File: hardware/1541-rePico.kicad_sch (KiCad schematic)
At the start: 10 parts, among them J1 Display Connector, J2 KEYS, J3 RESET_1541, J4 SD Card Module Connector, J5 EXT_5V, SW1 RESET, U1 Pico

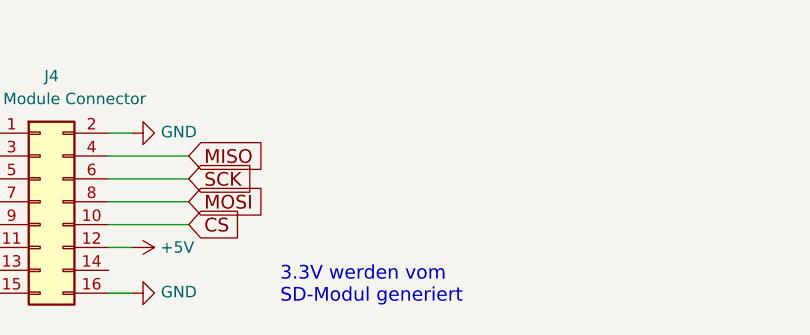
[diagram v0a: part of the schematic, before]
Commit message: updated PCB layout
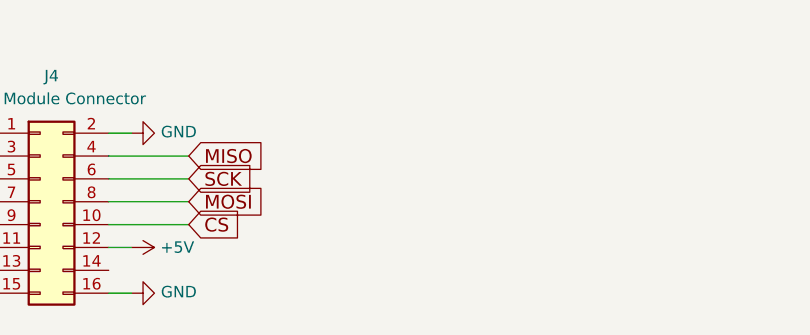
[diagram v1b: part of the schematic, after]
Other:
- note removed: "3.3V werden vom SD-Modul generiert"
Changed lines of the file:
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@@
     (stroke (width 0) (type default))
-  )
-  (text "3.3V werden vom\nSD-Modul generiert" (at 138.43 184.15 0)
-    (effects (font (size 1.524 1.524)) (justify left bottom))
   )
   (text "Jumper Normal offen" (at 241.3 105.41 0)

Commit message: updated schematics&pcb - version 1.1
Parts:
- removed J2: KEYS, Connector_PinHeader_2.54mm:PinHeader_1x04_P2.54mm_Vertical, symbol Connector_Generic:Conn_01x04
- added J2: Conn_02x03_Odd_Even, Connector_PinHeader_2.54mm:PinHeader_2x03_P2.54mm_Vertical, symbol Connector_Generic:Conn_02x03_Odd_Even
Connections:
- net BT1: now also J2.2 (Pin_2)
- net BT2: now also J2.4 (Pin_4)
- net BT3: now also J2.6 (Pin_6)
- net GND: now also J2.1 (Pin_1), J2.3 (Pin_3), J2.5 (Pin_5)

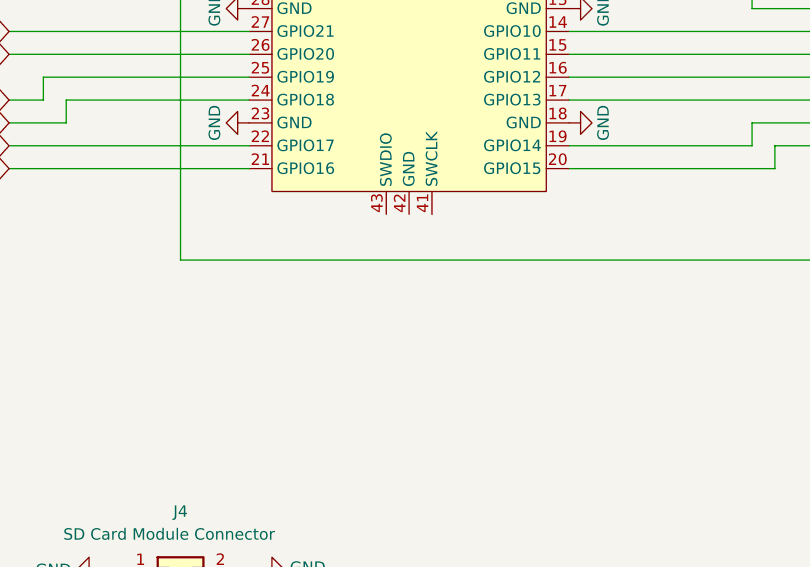
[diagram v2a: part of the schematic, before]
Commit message: fix WPS cross-driving
connection between 1541-board and VIA cut off
no cross driving of existing 74LS04 and Pico avoided
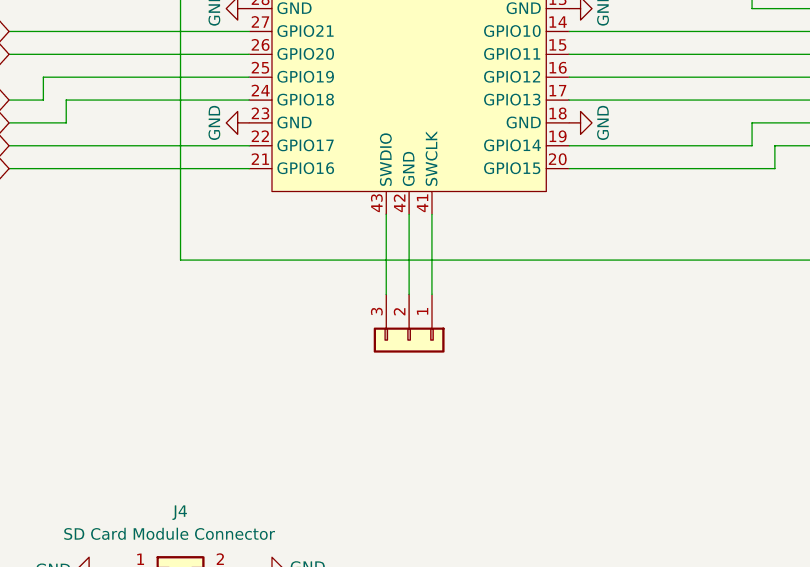
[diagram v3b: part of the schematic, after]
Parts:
- added SWDBG1: DEBUG, Connector_PinHeader_2.54mm:PinHeader_1x03_P2.54mm_Vertical, symbol Connector_Generic:Conn_01x03
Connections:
- net at U1.41 (SWCLK): now also SWDBG1.1 (Pin_1)
- net at U1.42 (GND): now also SWDBG1.2 (Pin_2)
- net at U1.43 (SWDIO): now also SWDBG1.3 (Pin_3)
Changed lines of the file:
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@@
+	(wire
+		(pts
+			(xy 140.97 125.73) (xy 140.97 134.62)
+		)
+		(stroke
+			(width 0)
+			(type default)
+		)
+	)
 	(wire
 		(pts
@@
 	(wire
 		(pts
+			(xy 138.43 125.73) (xy 138.43 134.62)
+		)
+		(stroke
+			(width 0)
+			(type default)
+		)
+	)
+	(wire
+		(pts
 			(xy 106.68 170.18) (xy 97.79 170.18)
 		)
@@
 		(pts
 			(xy 229.87 95.25) (xy 219.71 95.25)
+		)
+		(stroke
+			(width 0)
+			(type default)
+		)
+	)
+	(wire
+		(pts
+			(xy 135.89 125.73) (xy 135.89 134.62)
 		)
 		(stroke
@@
 					(unit 1)
 				)
+			)
+		)
+	)
+	(symbol
+		(lib_id "Connector_Generic:Conn_01x03")
+		(at 138.43 139.7 270)
+		(unit 1)
+		(exclude_from_sim no)
+		(in_bom yes)
+		(on_board yes)
+		(dnp no)
+		(property "Reference" "SWDBG1"
+			(at 143.51 139.7 90)
+			(effects
+				(font
+					(size 1.27 1.27)
+				)
+				(justify left)
+				(hide yes)
+			)
+		)
+		(property "Value" "DEBUG"
+			(at 138.43 142.24 90)
+			(effects
+				(font
+					(size 1.27 1.27)
+				)
+				(justify left)
+				(hide yes)
+			)
+		)
+		(property "Footprint" "Connector_PinHeader_2.54mm:PinHeader_1x03_P2.54mm_Vertical"
+			(at 138.43 139.7 0)
+			(effects
+				(font
+					(size 1.27 1.27)
+				)
+				(hide yes)
+			)
+		)
+		(property "Datasheet" "~"
+			(at 138.43 139.7 0)
+			(effects
+				(font
+					(size 1.27 1.27)
+				)
+				(hide yes)
+			)
+		)
+		(property "Description" ""
+			(at 138.43 139.7 0)
+			(effects
+				(font
+					(size 1.27 1.27)
+				)
+			)
+		)
+		(pin "1"
+		)
+		(pin "2"
+		)
+		(pin "3"
+		)
+		(instances
+			(project "1541-rePico"
+				(path "/7c37ffbe-d8d1-4c30-ad42-fd3ef959e14d"
+					(reference "SWDBG1")
+					(unit 1)
+				)
